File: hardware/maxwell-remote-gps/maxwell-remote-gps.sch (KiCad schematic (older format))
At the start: 11 parts, among them J1 IO, J2 UART1, U1 SC16IS752IPW, U2 FGPMMOPA6C, Y1 14.7456M

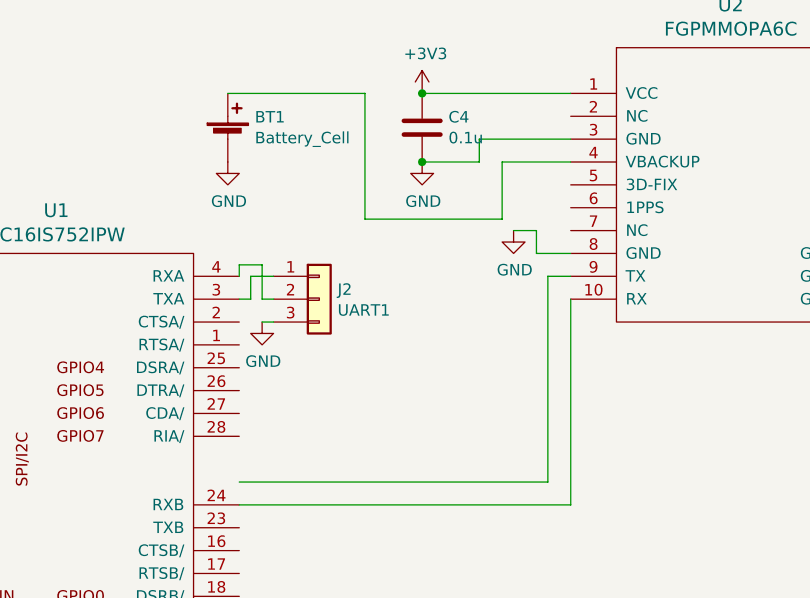
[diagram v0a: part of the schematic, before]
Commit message: Updating to include possible GPIOs for PPS and 3DFIX.
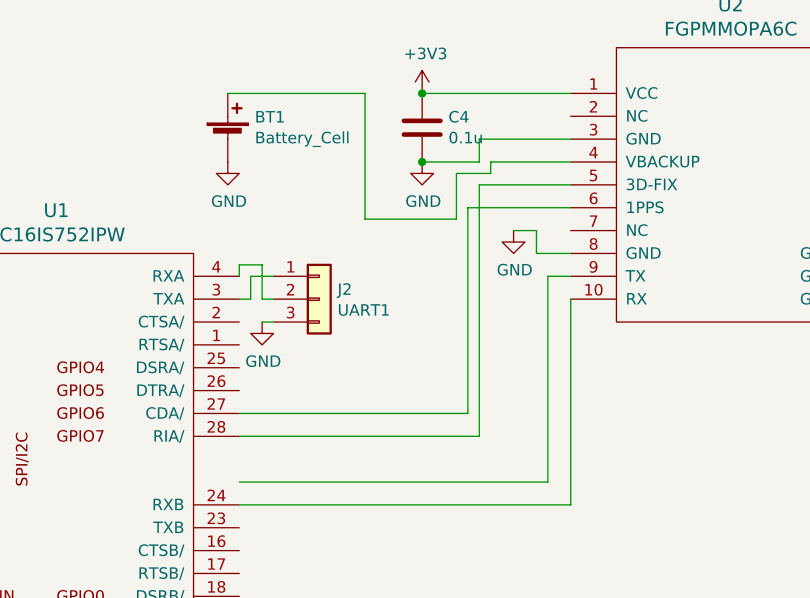
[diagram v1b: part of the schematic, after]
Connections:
- wire segments 53 -> 61
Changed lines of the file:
@@
 $EndComp
-Wire Wire Line
-	7250 1450 6950 1450
-Wire Wire Line
-	6950 1450 6950 1700
-Wire Wire Line
-	6950 1700 6350 1700
 Wire Wire Line
 	6350 1700 6350 1150
@@
 Wire Wire Line
 	5900 2050 5950 2050
+Wire Wire Line
+	6350 1700 6750 1700
+Wire Wire Line
+	6750 1700 6750 1500
+Wire Wire Line
+	6900 1500 6900 1450
+Wire Wire Line
+	6900 1450 7250 1450
+Wire Wire Line
+	6750 1500 6900 1500
+Wire Wire Line
+	6800 2550 5800 2550
+Wire Wire Line
+	5800 2650 6850 2650
+Wire Wire Line
+	7250 1550 6850 1550
+Wire Wire Line
+	6850 1550 6850 2650
+Wire Wire Line
+	6800 2550 6800 1650
+Wire Wire Line
+	6800 1650 7250 1650
 $EndSCHEMATC

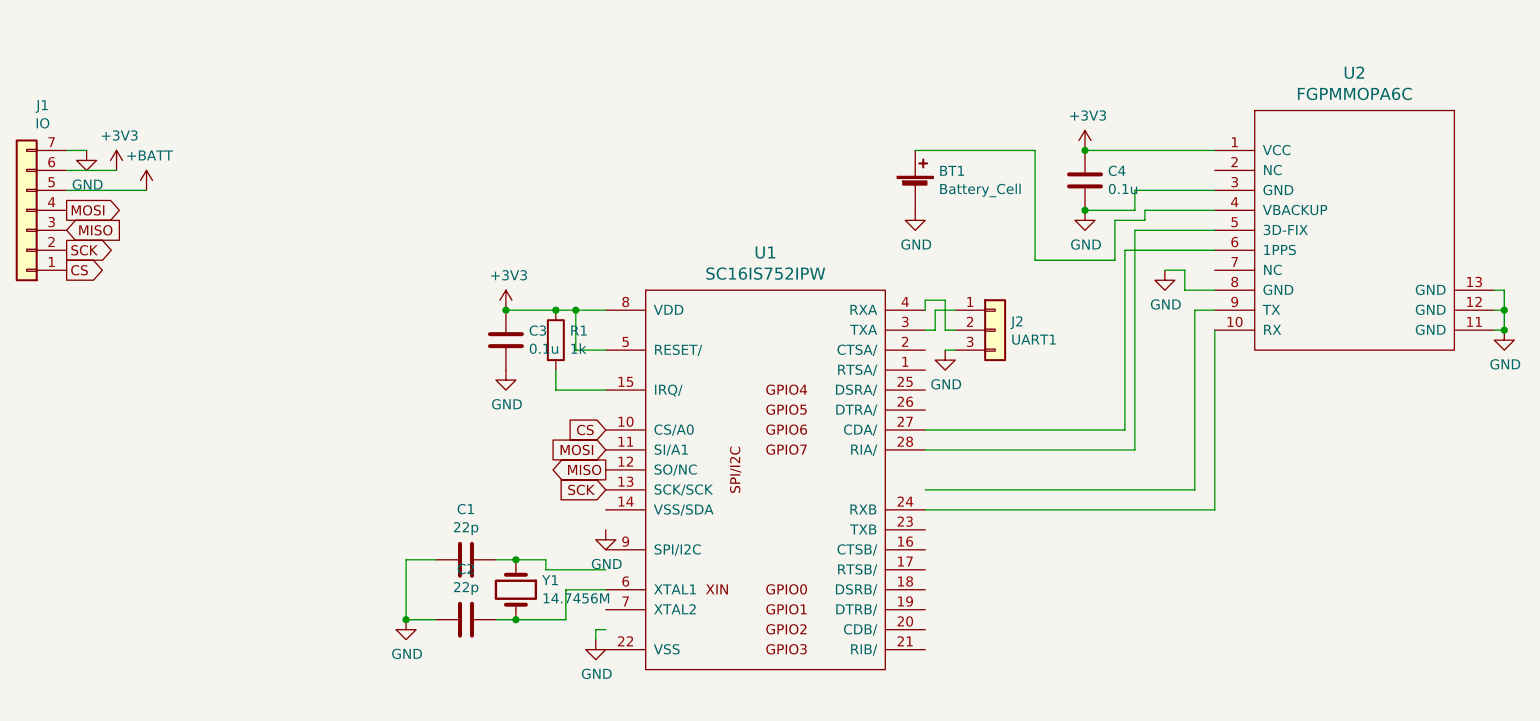
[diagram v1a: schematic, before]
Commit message: Updating maxwell-remote-gps to latest schematic and layout.
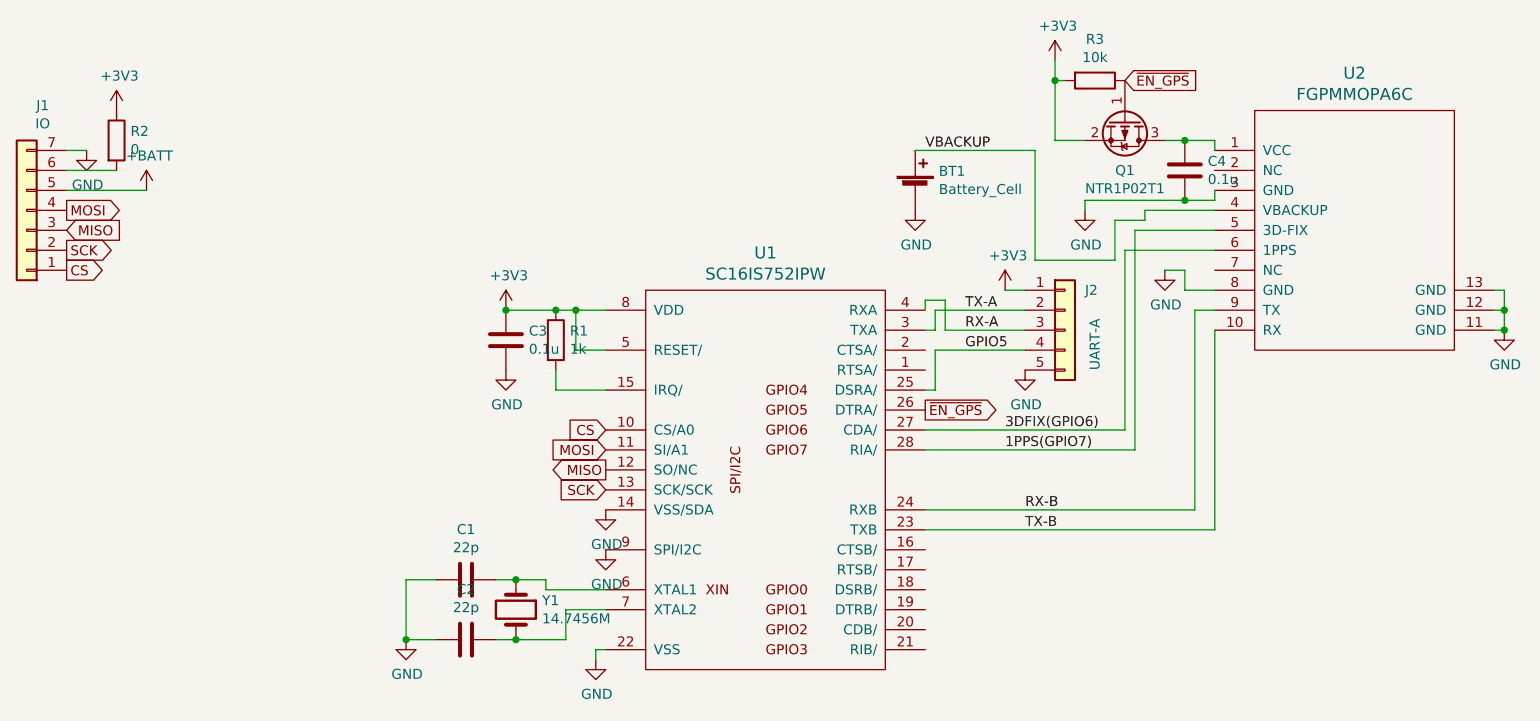
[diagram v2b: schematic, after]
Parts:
- removed J2: UART1, coddingtonbear:JST_EH_B03B-EH-A_03x2.50mm_Straight_LargePads, symbol Connector_Generic:Conn_01x03
- added J2: UART-A, coddingtonbear:JST_EH_B05B-EH-A_05x2.50mm_Straight_LargePads, symbol Connector_Generic:Conn_01x05
- added Q1: NTR1P02T1, coddingtonbear:SOT-23_LargePads, symbol Device:Q_PMOS_GSD
- added R2: 0, coddingtonbear:0805_Milling, symbol Device:R
- added R3: 10k, coddingtonbear:0805_Milling, symbol Device:R
- Y1: footprint Crystal:Crystal_HC49-U_Vertical -> coddingtonbear:Crystal_HC49-U_Vertical_LargePads
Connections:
- net labels added: 1PPS(GPIO7), 3DFIX(GPIO6), GPIO5, RX-A, RX-B, TX-A, TX-B, VBACKUP, ~EN_GPS
- wire segments 61 -> 71
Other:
- moved on the sheet: C1, C2, C4, Y1
